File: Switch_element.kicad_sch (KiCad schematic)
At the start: 9 parts, among them U901 AP22653AW6-7, U902 AP22653AW6-7

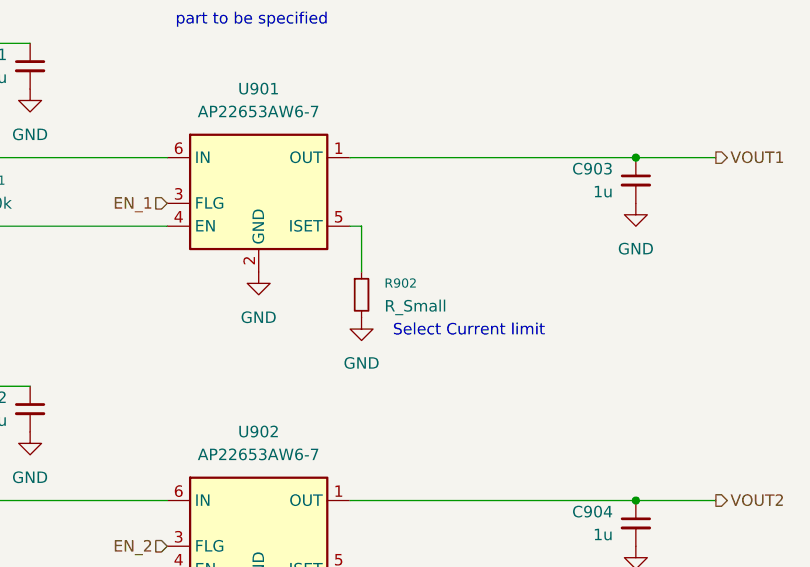
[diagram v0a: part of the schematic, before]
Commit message: connected CAN driver, added 3 solar inputs
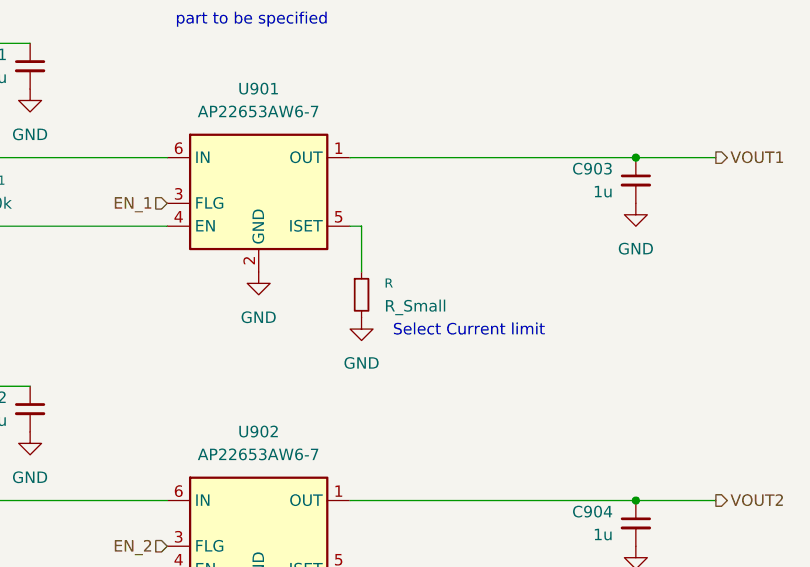
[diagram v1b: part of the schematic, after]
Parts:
- renumbered R902 to R

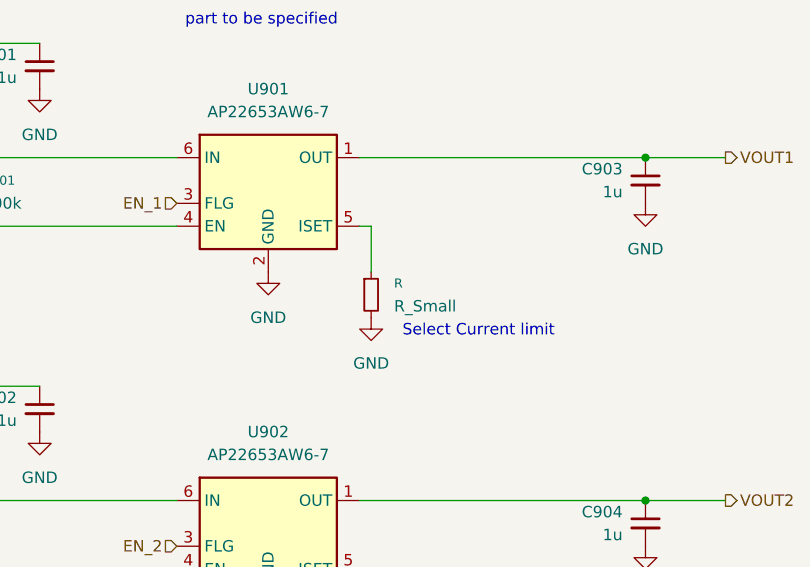
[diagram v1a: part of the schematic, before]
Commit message: added possible solutions for mppt
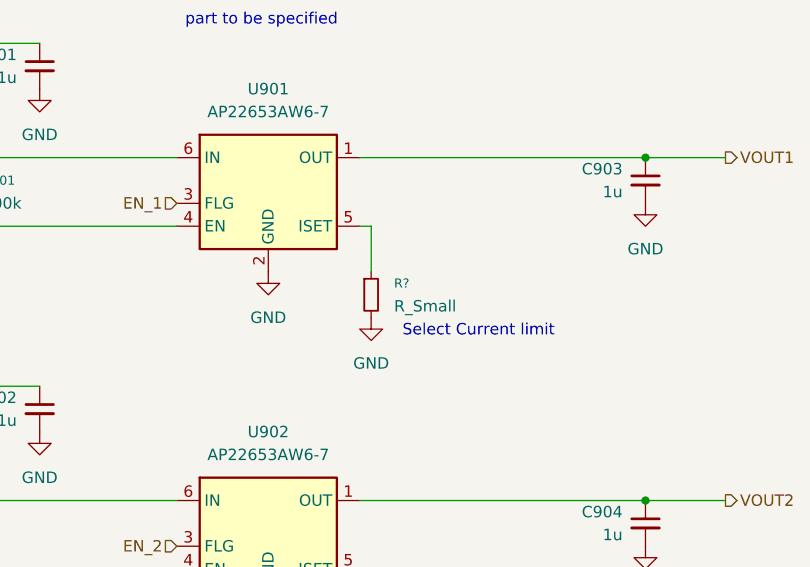
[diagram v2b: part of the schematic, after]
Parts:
- renumbered R to R?
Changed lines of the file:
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@@
 		(dnp no)
 		(fields_autoplaced yes)
-		(property "Reference" "R"
+		(property "Reference" "R?"
 			(at 158.75 92.7099 0)
 			(effects
@@
 		(instances
 			(project "EPS"
+				(path "/94201994-47b8-4213-8d1a-05da12b2a7b0/6db81d8c-9fb2-4091-8ea0-53a42b19d9d5/0a72ef8b-fc17-4425-a2e0-5d8a2bc4ee62"
+					(reference "R?")
+					(unit 1)
+				)
+				(path "/94201994-47b8-4213-8d1a-05da12b2a7b0/753d5f84-b54d-4af4-8110-8025fd55b679/0a72ef8b-fc17-4425-a2e0-5d8a2bc4ee62"
+					(reference "R?")
+					(unit 1)
+				)
+				(path "/94201994-47b8-4213-8d1a-05da12b2a7b0/ab44f8e8-c8ba-43e8-b5cb-dd05d8d64fc9/0a72ef8b-fc17-4425-a2e0-5d8a2bc4ee62"
+					(reference "R?")
+					(unit 1)
+				)
+				(path "/94201994-47b8-4213-8d1a-05da12b2a7b0/c5b5e45e-bc62-4324-a083-6950b16f429f/0a72ef8b-fc17-4425-a2e0-5d8a2bc4ee62"
+					(reference "R?")
+					(unit 1)
+				)
+				(path "/94201994-47b8-4213-8d1a-05da12b2a7b0/2806d1e0-46ba-47ac-8022-17737bffb744/594e15f8-4e85-4fe0-b465-2b21bea5b847/0a72ef8b-fc17-4425-a2e0-5d8a2bc4ee62"
+					(reference "R?")
+					(unit 1)
+				)
 				(path "/94201994-47b8-4213-8d1a-05da12b2a7b0/4e89c933-7889-465d-8e1a-713a5947b2aa/50b5827b-91e2-4f95-b489-8fc588047e5c/0a72ef8b-fc17-4425-a2e0-5d8a2bc4ee62"
 					(reference "R7502")
@@
 				(path "/94201994-47b8-4213-8d1a-05da12b2a7b0/4e89c933-7889-465d-8e1a-713a5947b2aa/b7b15344-d852-4d94-8b9c-7ad6d1607b83/0a72ef8b-fc17-4425-a2e0-5d8a2bc4ee62"
 					(reference "R7702")
+					(unit 1)
+				)
+				(path "/94201994-47b8-4213-8d1a-05da12b2a7b0/80284205-18d0-4824-96a2-1f6126c1d232/50b5827b-91e2-4f95-b489-8fc588047e5c/0a72ef8b-fc17-4425-a2e0-5d8a2bc4ee62"
+					(reference "R?")
+					(unit 1)
+				)
+				(path "/94201994-47b8-4213-8d1a-05da12b2a7b0/80284205-18d0-4824-96a2-1f6126c1d232/b7b15344-d852-4d94-8b9c-7ad6d1607b83/0a72ef8b-fc17-4425-a2e0-5d8a2bc4ee62"
+					(reference "R?")
+					(unit 1)
+				)
+				(path "/94201994-47b8-4213-8d1a-05da12b2a7b0/8920358c-844b-40af-9382-a9a47367f2f9/18317d81-3057-4f2d-8dd0-207e3d519bfa/508fc56f-a02d-42ca-801d-9d175147305c"
+					(reference "R?")
+					(unit 1)
+				)
+				(path "/94201994-47b8-4213-8d1a-05da12b2a7b0/8920358c-844b-40af-9382-a9a47367f2f9/2ce2f176-9fe8-4061-8c39-1923e057ed0c/508fc56f-a02d-42ca-801d-9d175147305c"
+					(reference "R?")
+					(unit 1)
+				)
+				(path "/94201994-47b8-4213-8d1a-05da12b2a7b0/8920358c-844b-40af-9382-a9a47367f2f9/2f976210-1750-43d6-9de2-2df7b908e425/0a72ef8b-fc17-4425-a2e0-5d8a2bc4ee62"
+					(reference "R?")
+					(unit 1)
+				)
+				(path "/94201994-47b8-4213-8d1a-05da12b2a7b0/8920358c-844b-40af-9382-a9a47367f2f9/4f021f1d-bda8-4e33-8695-9d319bdd93ab/508fc56f-a02d-42ca-801d-9d175147305c"
+					(reference "R?")
+					(unit 1)
+				)
+				(path "/94201994-47b8-4213-8d1a-05da12b2a7b0/8920358c-844b-40af-9382-a9a47367f2f9/8713cb3d-d236-4b25-b8f7-c3a74cdfa63c/508fc56f-a02d-42ca-801d-9d175147305c"
+					(reference "R?")
+					(unit 1)
+				)
+				(path "/94201994-47b8-4213-8d1a-05da12b2a7b0/8920358c-844b-40af-9382-a9a47367f2f9/8c53dc13-be93-4284-a23f-1625eb6681cf/508fc56f-a02d-42ca-801d-9d175147305c"
+					(reference "R?")
+					(unit 1)
+				)
+				(path "/94201994-47b8-4213-8d1a-05da12b2a7b0/8920358c-844b-40af-9382-a9a47367f2f9/9671229e-fdfa-4b19-b847-02c627725d01/508fc56f-a02d-42ca-801d-9d175147305c"
+					(reference "R?")
+					(unit 1)
+				)
+				(path "/94201994-47b8-4213-8d1a-05da12b2a7b0/8920358c-844b-40af-9382-a9a47367f2f9/a0428678-92cf-415e-aa00-fdfb19916946/508fc56f-a02d-42ca-801d-9d175147305c"
+					(reference "R?")
+					(unit 1)
+				)
+				(path "/94201994-47b8-4213-8d1a-05da12b2a7b0/8920358c-844b-40af-9382-a9a47367f2f9/bd8c69bd-d91d-4583-9982-b77bd13f9b29/0a72ef8b-fc17-4425-a2e0-5d8a2bc4ee62"
+					(reference "R?")
+					(unit 1)
+				)
+				(path "/94201994-47b8-4213-8d1a-05da12b2a7b0/8920358c-844b-40af-9382-a9a47367f2f9/dd2c750e-def6-42fd-86ab-835d368529b5/508fc56f-a02d-42ca-801d-9d175147305c"
+					(reference "R?")
+					(unit 1)
+				)
+				(path "/94201994-47b8-4213-8d1a-05da12b2a7b0/b0e1f780-fe26-45de-bffd-6cbe93fb90fd/50b5827b-91e2-4f95-b489-8fc588047e5c/0a72ef8b-fc17-4425-a2e0-5d8a2bc4ee62"
+					(reference "R?")
+					(unit 1)
+				)
+				(path "/94201994-47b8-4213-8d1a-05da12b2a7b0/b0e1f780-fe26-45de-bffd-6cbe93fb90fd/b7b15344-d852-4d94-8b9c-7ad6d1607b83/0a72ef8b-fc17-4425-a2e0-5d8a2bc4ee62"
+					(reference "R?")
+					(unit 1)
+				)
+				(path "/94201994-47b8-4213-8d1a-05da12b2a7b0/b1cfc9a6-bdf2-4ebb-ae2c-6da62e7f592e/50b5827b-91e2-4f95-b489-8fc588047e5c/0a72ef8b-fc17-4425-a2e0-5d8a2bc4ee62"
+					(reference "R?")
+					(unit 1)
+				)
+				(path "/94201994-47b8-4213-8d1a-05da12b2a7b0/b1cfc9a6-bdf2-4ebb-ae2c-6da62e7f592e/b7b15344-d852-4d94-8b9c-7ad6d1607b83/0a72ef8b-fc17-4425-a2e0-5d8a2bc4ee62"
+					(reference "R?")
 					(unit 1)
 				)
@@
 					(unit 1)
 				)
+				(path "/94201994-47b8-4213-8d1a-05da12b2a7b0/d95d278d-1c38-4dd0-90b4-8a93da58da95/594e15f8-4e85-4fe0-b465-2b21bea5b847/0a72ef8b-fc17-4425-a2e0-5d8a2bc4ee62"
+					(reference "R?")
+					(unit 1)
+				)

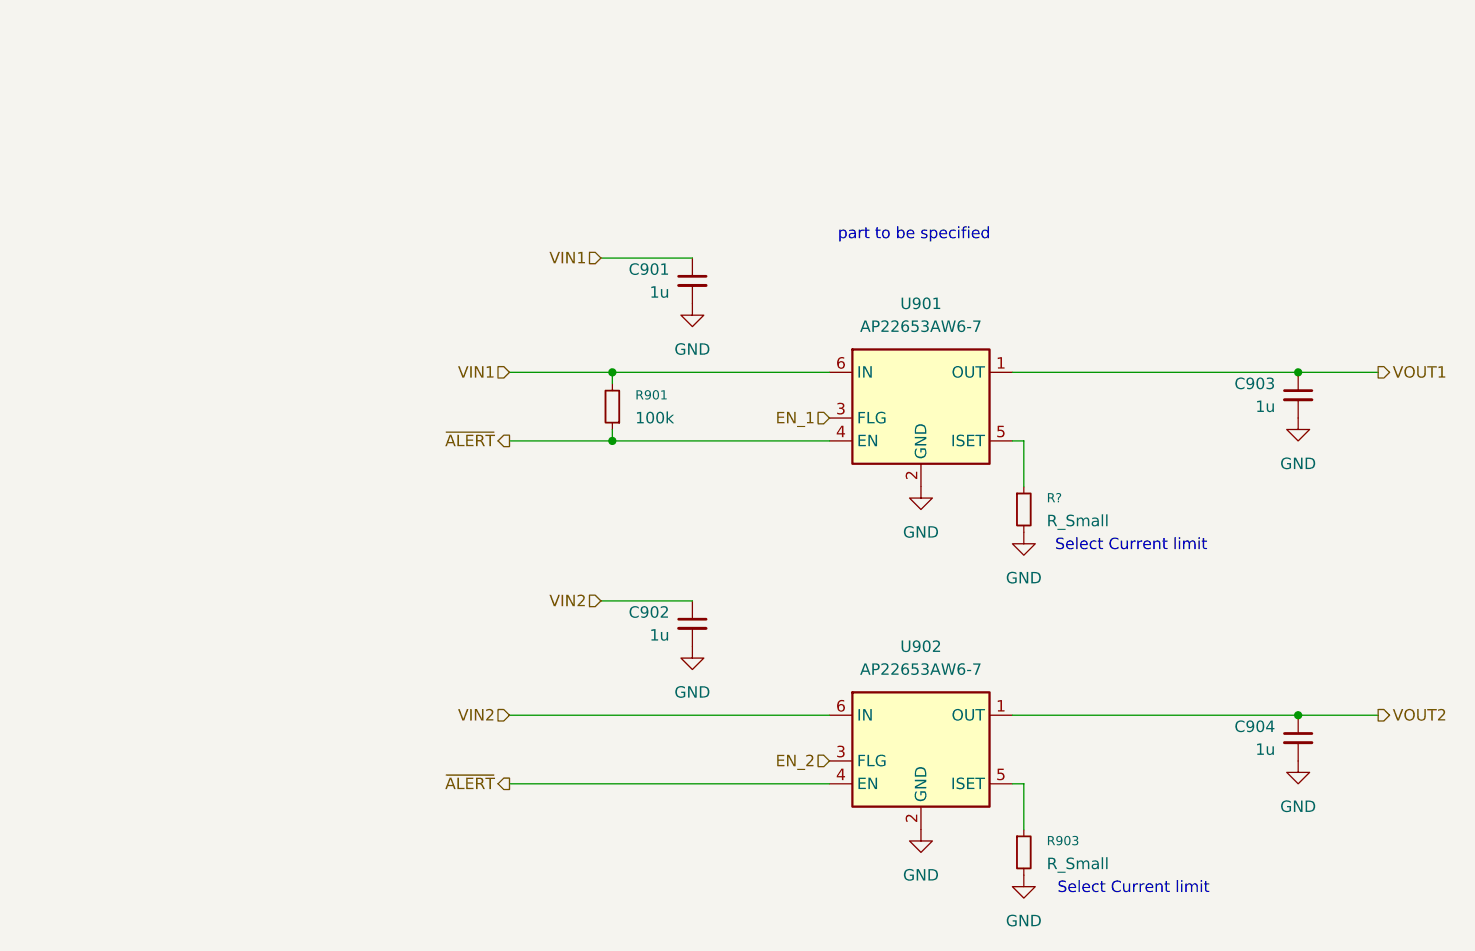
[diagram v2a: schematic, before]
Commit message: updated battery pack module; updated solar inputs module
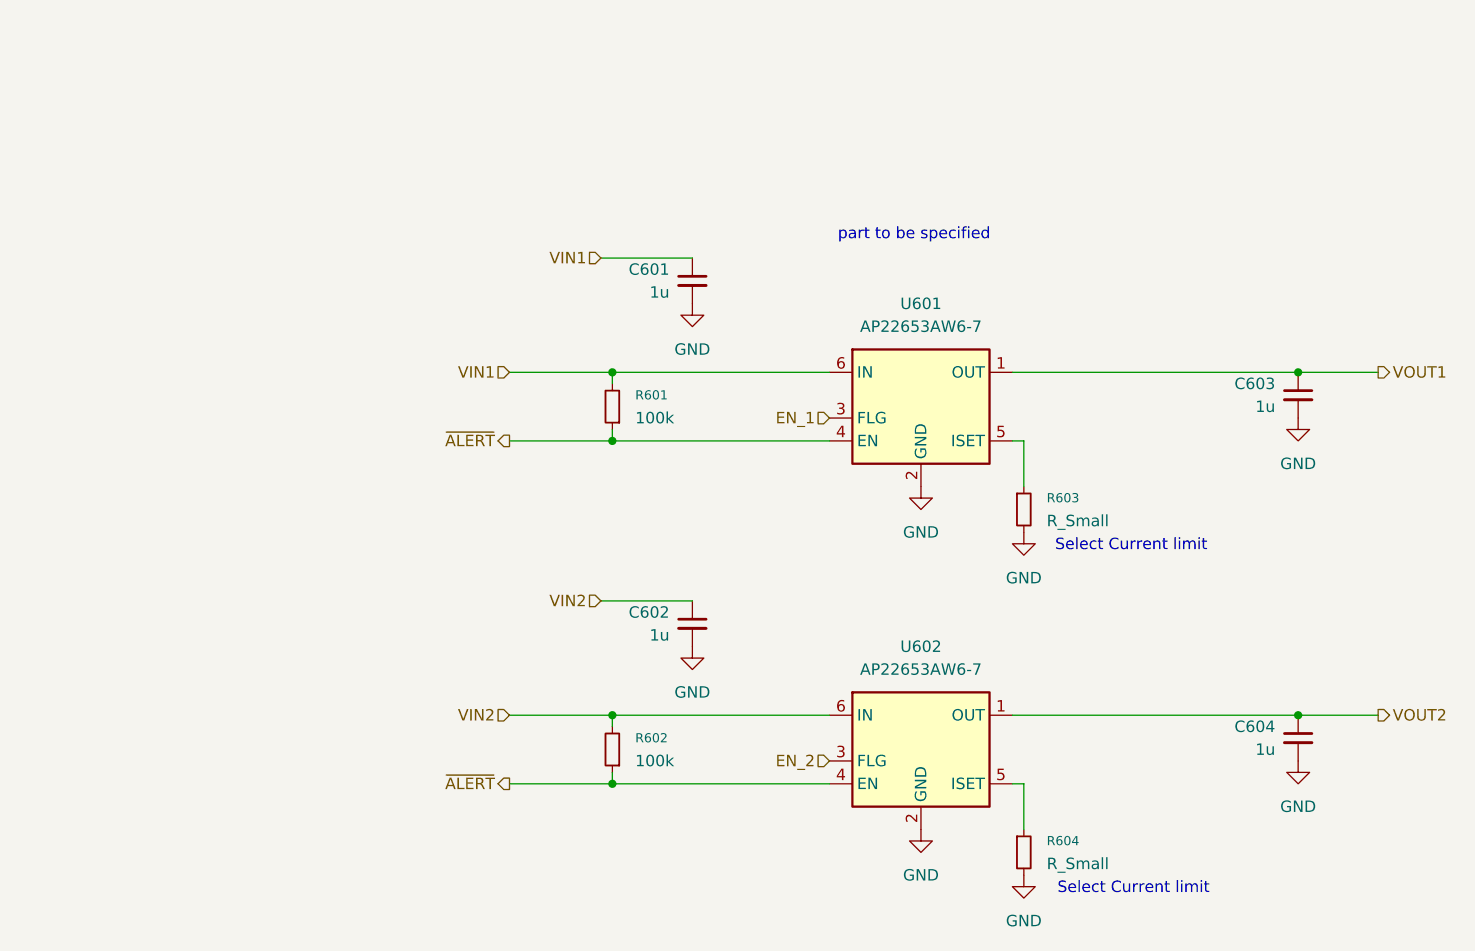
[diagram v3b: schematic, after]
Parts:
- added R602: 100k, Resistor_SMD:R_0603_1608Metric_Pad0.98x0.95mm_HandSolder, symbol Device:R_Small
- gave numbers to parts that had none: 1
- renumbered C901 to C601, C902 to C602, C903 to C603, C904 to C604, R901 to R601, R903 to R604, U901 to U601, U902 to U602
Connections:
- net VIN2: now also R602.2
- net ~{ALERT}: now also R602.1

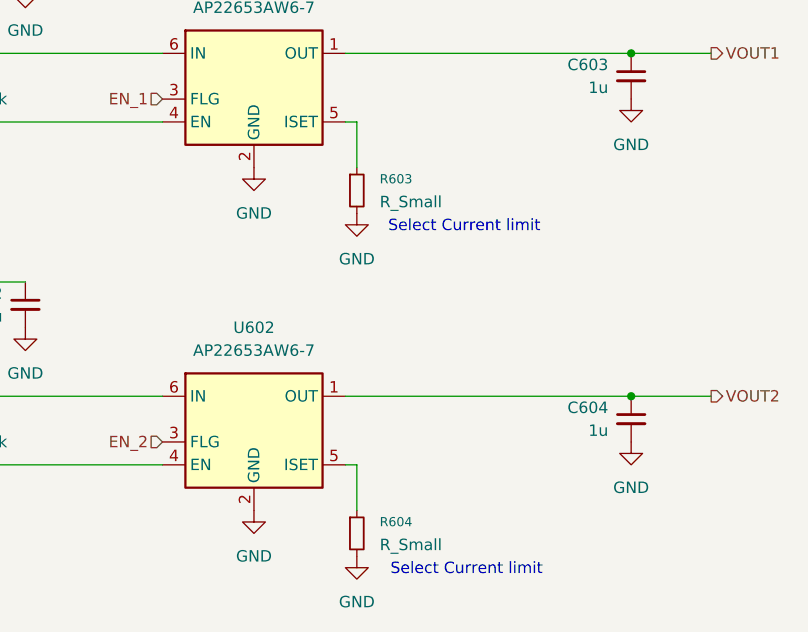
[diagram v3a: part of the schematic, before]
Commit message: added values to most parts
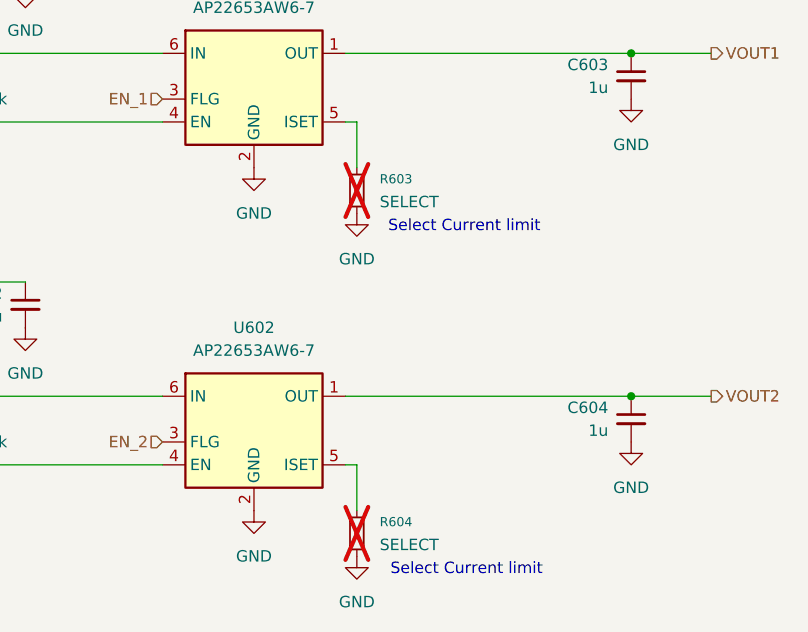
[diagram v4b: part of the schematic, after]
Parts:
- R603, R604: value R_Small -> SELECT; now not fitted
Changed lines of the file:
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@@
 		(in_bom yes)
 		(on_board yes)
-		(dnp no)
+		(dnp yes)
 		(fields_autoplaced yes)
 		(property "Reference" "R604"
@@
 			)
 		)
-		(property "Value" "R_Small"
+		(property "Value" "SELECT"
 			(at 158.75 133.3499 0)
 			(effects
@@
 		(in_bom yes)
 		(on_board yes)
-		(dnp no)
+		(dnp yes)
 		(fields_autoplaced yes)
 		(property "Reference" "R603"
@@
 			)
 		)
-		(property "Value" "R_Small"
+		(property "Value" "SELECT"
 			(at 158.75 95.2499 0)
 			(effects
